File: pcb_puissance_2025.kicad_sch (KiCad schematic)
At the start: 25 parts, among them J1 1755736, J2 1755736, J3 1755736, J4 1755736, J5 1755736, J6 1755736

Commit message: PCB 2025 rev2
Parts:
- added TP1, TP2, TP3, TP4, TP5, TP6, TP7, TP8: TestPoint, TestPoint:TestPoint_Pad_D1.5mm, symbol Connector:TestPoint
- renumbered F6 to F5, F5 to F6
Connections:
- net 3V3: now also TP3.1
- net GND: now also TP1.1
- net power_input_selector/VOUT: now also TP2.1
- net at F6.2, PS3.1 (+VIN_(VCC)): now also TP6.1
- net at F7.2, PS4.1 (+VIN_(VCC)): now also TP7.1
- net at F4.2, PS5.1 (+VIN_(VCC)): now also TP4.1
- net at F5.2, PS2.1 (+VIN_(VCC)): now also TP5.1
- net at F8.2, PS1.2 (+VIN_(VCC)): now also TP8.1
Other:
- moved on the sheet: F1, F2, F3, F4, F5, F6, F7, F8, J4, J5, PS1, PS2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

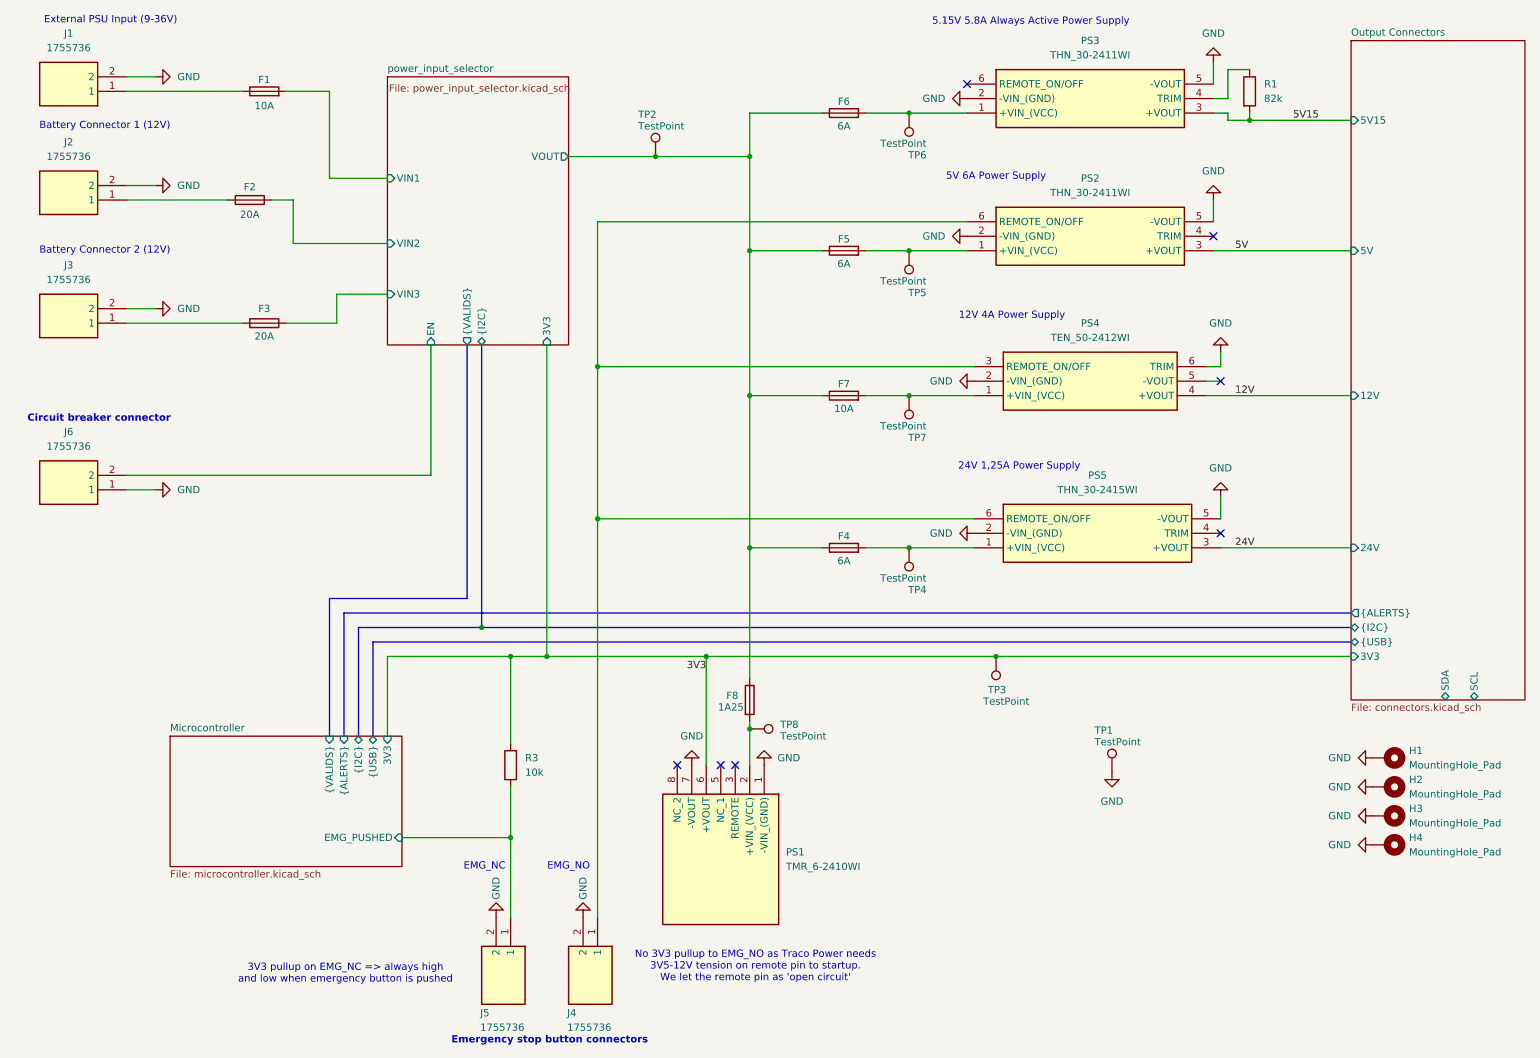
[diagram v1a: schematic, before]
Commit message: nouvelle version : correction erreurs, ameliorations qualite, passage a 4 couches, ajout pilotage des traco depuis le stm32
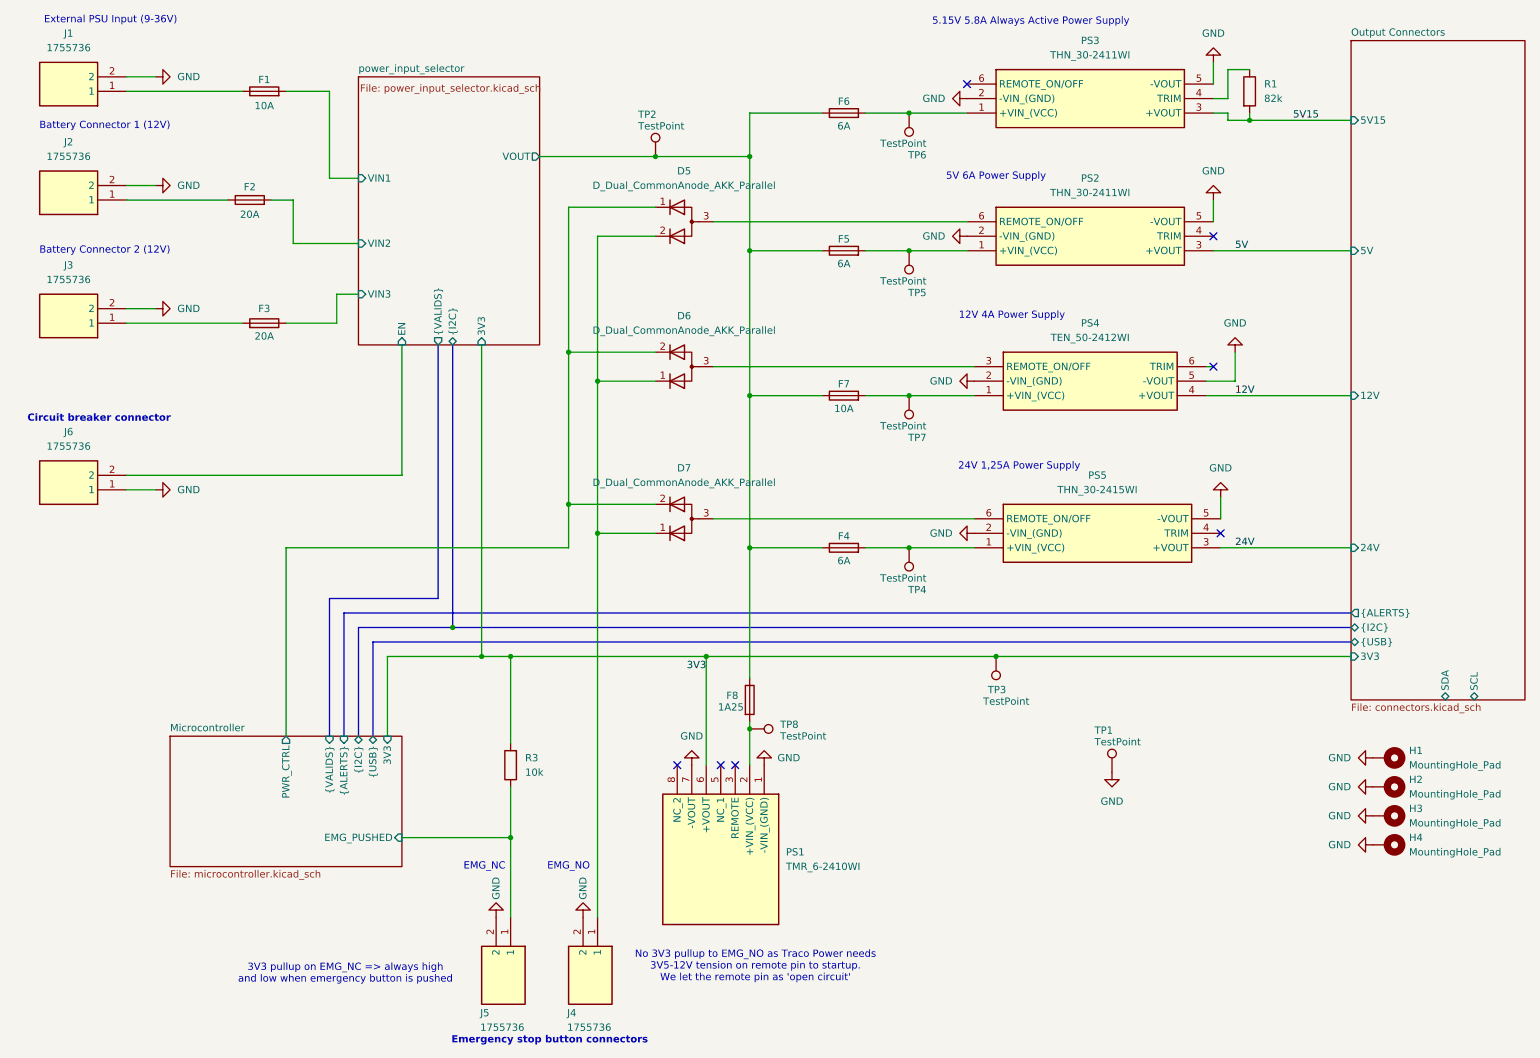
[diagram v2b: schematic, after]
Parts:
- added D5, D6, D7: D_Dual_CommonAnode_AKK_Parallel, Package_TO_SOT_SMD:TSOT-23_HandSoldering, symbol Device:D_Dual_CommonAnode_AKK_Parallel
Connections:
- net GND: now also PS4.5 (-VOUT); no longer PS4.6 (TRIM)
- new net: D6.3 (A), PS4.3 (REMOTE_ON/OFF)
- new net: D5.2 (K), D6.1 (K), D7.1 (K), J4.1
- new net: D5.3 (A), PS2.6 (REMOTE_ON/OFF)
- new net: D7.3 (A), PS5.6 (REMOTE_ON/OFF)
- new net Microcontroller/PWR_CTRL: D5.1 (K), D6.2 (K), D7.2 (K)
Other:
- sheet Microcontroller ports: added PWR_CTRL; removed none
